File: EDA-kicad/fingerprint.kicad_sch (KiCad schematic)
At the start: 2 parts, among them J4 FINGER

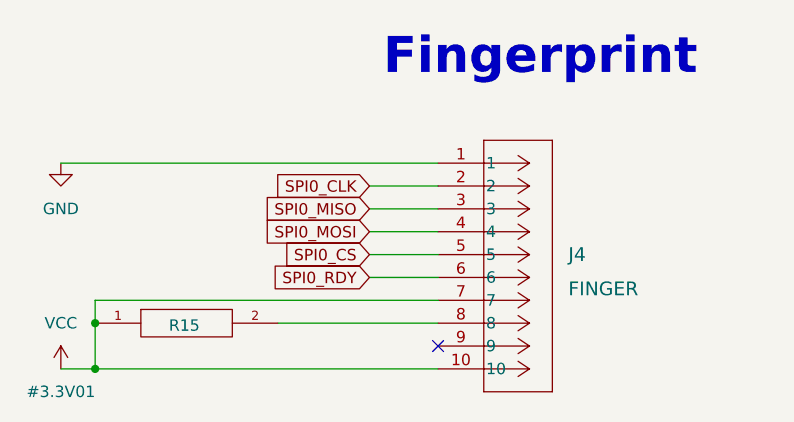
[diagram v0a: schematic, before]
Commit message: reannotate entire schematic
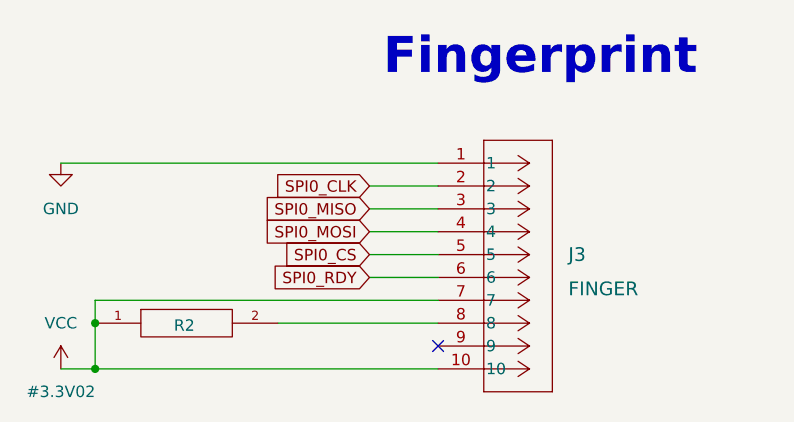
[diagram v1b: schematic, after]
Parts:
- renumbered J4 to J3, R15 to R2
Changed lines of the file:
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@@
 			"AAAAAAAAAAAAAAAAAAAAAAAAAAAAAAAAAAAAAAAAAAAAAAAAAAAAAAAAAAAAAAAAAAAAAAAAAAAA"
 			"AAAAAAAAAAAAAAAAAAAAAAAAAAAAAAAAAAAAAAAAAAAAAAAAAAAAAAAAAAAAAAAAAAAAAAAAAAAA"
-			"AAAAAAAAAAAAAAAAAAAAAAAAAAAAAAAAAAAAAAAAAAAAAAAAAAAAAA=="
+			"AAAAAAAAAAAAAAAAAAAAAAAAAAAAAAAAAAAAAAAAAAAAAAAAAAAAAAAAAFBCJC1WVQAACQAAAAAA"
+			"AAAJAAAAAAAAAEMAAABvAAAAAAAAAAAAAAAAAAAAAAAAACDDqylWVQAAFAAAAAAAAAAUAAAAAAAA"
+			"AEwAAAA3AAAAAAAAAAAAAAAAAAAAAAAAADYAAAA4AAAAkQAAAAAAAABwViQtVlUAAMAcX/oZfwAA"
+			"oFQkLVZVAACAViQtVlUAAMBJJC1WVQAACQAAAAAAAAAJAAAAAAAAAIBZa/QYfwAAAAAAAAAAAAAA"
+			"AAAAAAAAACBWJC1WVQAAAQAAAAAAAABVAAAAAAAAAEEAAABMAAAAAAAAAAAAAAAAAAAAAAAAAEAC"
+			"AAAAAAAAMAAAAAAAAAA1kEZ4U1UAAENoYXJhY3RlcgAAAGgAAABlAAAAZQAAAHQAAAAAAAAA0QcA"
+			"AAAAAABwwCMTVlUAAOCxJC1WVQAAAAAAAAAAAAAAAAAAAAAAACCf8yRWVQAABQAAAAAAAAAFAAAA"
+			"AAAAAHcAAAB3AAAAAAAAAAAAAAAAAAAAAAAAAJBTJC1WVQAADAAAAAAAAAAMAAAAAAAAAHQAAAAu"
+			"AAAAAAAAAAAAAAAAAAAAAAAAAJAAAAAAAAAAUAEAAAAAAABHAAAAcgAAAGUAAABlAAAAbgAAACAA"
+			"AABTAAAAaQAAAG4AAABnAAAAbAAAAGUAAAAtAAAAZAAAAGkAAABnAAAAaQAAAHQAAAAgAAAATgAA"
+			"AHUAAABtAAAAZQAAAHIAAABpAAAAYwAAACAAAABEAAAAaQAAAHMAAABwAAAAbAAAAGEAAAB5AAAA"
+			"IAAAAHcAAABpAAAAdAAAAGgAAAAgAAAAdwAAAGgAAABpAAAAdAAAAGUAAAAgAAAAdwAAAGgAAABp"
+			"AAAAdAAAAGUAAAAgAAAAZAAAAGkAAABmAAAAZgAAAHUAAABzAAAAZQAAAGQAAAAgAAAAbAAAAGUA"
+			"AABuAAAAcwAAACwAAAAgAAAAYwAAAG8AAABtAAAAbQAAAG8AAABuAAAAIAAAAGEAAABuAAAAbwAA"
+			"AGQAAABlAAAAAAAAAHQAAABwAAAAEQEAAAAAAACAoiQtVlUAAMCUJC1WVQAAOgAAAC8AAAAvAAAA"
+			"dwAAAHcAAAB3AAAALgAAAGsAAABpAAAAbgAAAGcAAABiAAAAcgAAAGkAAABnAAAAaAAAAHQAAAB1"
+			"AAAAcwAAAGEAAAAuAAAAYwAAAG8AAABtAAAALwAAAGkAAABtAAAAYQAAAGcAAABlAAAAcwAAAC8A"
+			"AABjAAAAYQAAAHQAAABhAAAAbAAAAG8AAABnAAAALwAAAFMAAABQAAAARQAAAEMAAAAvAAAAUwAA"
+			"AEEAAAAxAAAANQAAAC0AAAAxAAAAMQAAAEUAAABXAAAAQQAAAC4AAA=="
 		)
 	)
@@
 			"AAAAAAAAAAAAAAAAAAAAAAAAAAAAAAAAAAAAAAAAAAAAAAAAAAAAAAAAAAAAAAAAAAAAAAAAAAAA"
 			"AAAAAAAAAAAAAAAAAAAAAAAAAAAAAAAAAAAAAAAAAAAAAAAAAAAAAAAAAAAAAAAAAAAAAAAAAAAA"
+			"AAAAAAAAAAAAAAAAAAAAAAAAAAAAAAAAAAAAAAAAAAAAAAAAAAAAAAAAAAAAAAAAAAAAAAAAAAAA"
+			"AAAAAAAAAAAAAAAAAAAAAAAAAAAAAAAAAAAAAAAAAAAAAAAAAAAAAAAAAAAAAAAAAAAAAAAAAAAA"
+			"AAAAAAAAAAAAAAAAAAAAAAAAAAAAAAAAAAAAAAAAAAAAAAAAAAAAAAAAAAAAAAAAAAAAAAAAAAAA"
+			"AAAAAAAAAAAAAAAAAAAAAAAAAAAAAAAAAAAAAAAAAAAAAAAAAAAAAAAAAAAAAAAAAAAAAAAAAAAA"
+			"AAAAAAAAAAAAAAAAAAAAAAAAAAAAAAAAAAAAAAAAAAAAAAAAAAAAAAAAAAAAAAAAAAAAAAAAAAAA"
+			"AAAAAAAAAAAAAAAAAAAAAAAAAAAAAAAAAAAAAAAAAAAAAAAAAAAAAAAAAAAAAAAAAAAAAAAAAAAA"
+			"AAAAAAAAAAAAAAAAAAAAAAAAAAAAAAAAAAAAAAAAAAAAAAAAAAAAAAAAAAAAAAAAAAAAAAAAAAAA"
+			"AAAAAAAAAAAAAAAAAAAAAAAAAAAAAAAAAAAAAAAAAAAAAAAAAAAAAAAAAAAAAAAAAAAAAAAAAAAA"
+			"AAAAAAAAAAAAAAAAAAAAAAAAAAAAAAAAAAAAAAAAAAAAAAAAAAAAAAAAAAAAAAAAAAAAAAAAAAAA"
+			"AAAAAAAAAAAAAAAAAAAAAAAAAAAAAAAAAAAAAAAAAAAAAAAAAAAAAAAAAAAAAAAAAAAAAAAAAAAA"
+			"AAAAAAAAAAAAAAAAAAAAAAAAAAAAAAAAAAAAAAAAAAAAAAAAAAAAAAAAAAAAAAAAAAAAAAAAAP//"
+			"/wHh0toi4dLaIt/P3yAAAAAAAAAAAAAAAAAAAAAAAAAAAAAAAAAAAAAAAAAAAAAAAAAAAAAAAAAA"
+			"AAAAAAAAAAAAAAAAAAAAAAAAAAAAAAAAAAAAAAAAAAAAAAAAAAAAAAAAAAAAAAAAAAAAAAAAAAAA"
+			"AAAAAAAAAAAAAAAAAAAAAAAAAAAAAAAAAAAAAAAAAAAAAAAAAAAAAAAAAAAAAAAAAAAAAN7T3nre"
+			"093a3tPcqd/f3wgAAAAAAAAAAOjR6Ave093/3tPd/97T3fIAAAAAAAAAAAAAAAAAAAAAAAAAAAAA"
+			"AAAAAAAAAAAAAAAAAAAAAAAAAAAAAAAAAAAAAAAAAAAAAAAAAAAAAAAAAAAAAAAAAAAAAAAAAAAA"
+			"AAAAAAAAAAAAAAAAAAAAAAAAAAAAAAAAAAAAAAAAAAAAAAAAAAAAAAAAAAAAAAAAAAAAAAAAAAAA"
+			"AAAAAAAAAAAAAAAA////Ad7T3fje093/3tPd/+DU3EEAAAAAAAAAAOjR6Ave093/3tPd/97T3fIA"
 			"AAAAAAAAAAAAAAAAAAAAAAAAAAAAAAAAAAAAAAAAAAAAAAAAAAAAAAAAAAAAAAAAAA=="
 		)
@@
 		(dnp no)
 		(fields_autoplaced yes)
-		(property "Reference" "#PWR01"
+		(property "Reference" "#PWR065"
 			(at 87.63 100.33 0)
 			(effects
@@
 			(project "cm5-carrier"
 				(path "/28c5e4fe-1ec7-4477-97f0-d2ec1401fad5/22a7f479-b60d-43d3-acd2-a72a0c1ab82c"
-					(reference "#PWR01")
+					(reference "#PWR065")
 					(unit 1)
 				)
@@
 		(on_board yes)
 		(dnp no)
-		(property "Reference" "#3.3V01"
+		(property "Reference" "#3.3V02"
 			(at 87.63 119.38 0)
 			(effects
@@
 			(project "cm5-carrier"
 				(path "/28c5e4fe-1ec7-4477-97f0-d2ec1401fad5/22a7f479-b60d-43d3-acd2-a72a0c1ab82c"
-					(reference "#3.3V01")
+					(reference "#3.3V02")
 					(unit 1)
 				)
@@
 		(dnp no)
 		(fields_autoplaced yes)
-		(property "Reference" "J4"
+		(property "Reference" "J3"
 			(at 144.018 104.14 0)
 			(effects
@@
 			(project "cm5-carrier"
 				(path "/28c5e4fe-1ec7-4477-97f0-d2ec1401fad5/22a7f479-b60d-43d3-acd2-a72a0c1ab82c"
-					(reference "J4")
+					(reference "J3")
 					(unit 1)
 				)
@@
 		(on_board yes)
 		(dnp no)
-		(property "Reference" "R15"
+		(property "Reference" "R2"
 			(at 101.346 112.014 0)
 			(effects
@@
 			(project "cm5-carrier"
 				(path "/28c5e4fe-1ec7-4477-97f0-d2ec1401fad5/22a7f479-b60d-43d3-acd2-a72a0c1ab82c"
-					(reference "R15")
+					(reference "R2")
 					(unit 1)
 				)

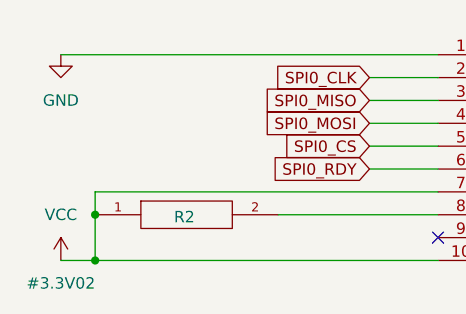
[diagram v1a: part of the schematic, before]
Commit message: add new switches and reannotate
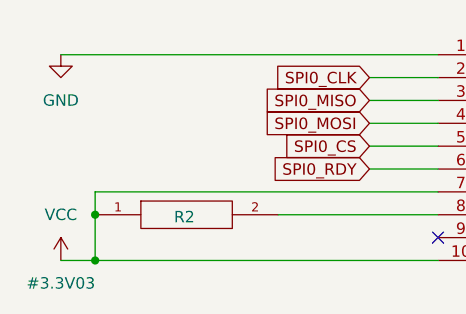
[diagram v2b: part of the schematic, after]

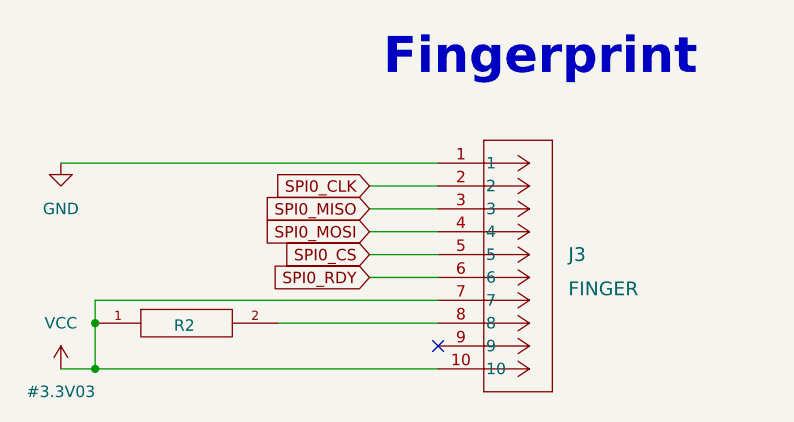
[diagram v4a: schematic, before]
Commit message: set everything except from power to DNP
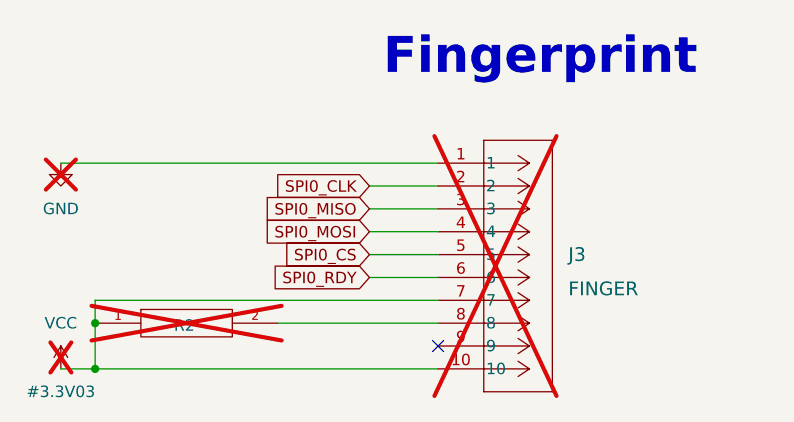
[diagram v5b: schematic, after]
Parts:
- J3, R2: now not fitted

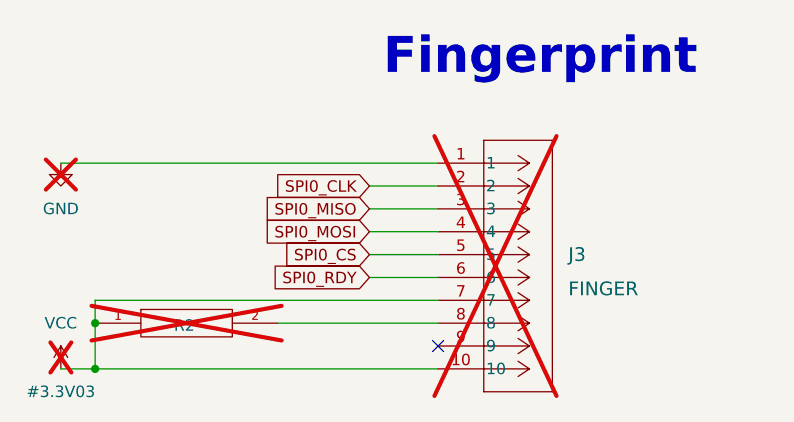
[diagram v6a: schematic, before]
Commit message: Improve KiCAD schematic design and labeling
- Replace overused global labels with hierarchical and local labels
- Add proper GND connections to components
- Fix BACKLIGHT- net issues
- Apply minor schematic fixes and cleanups
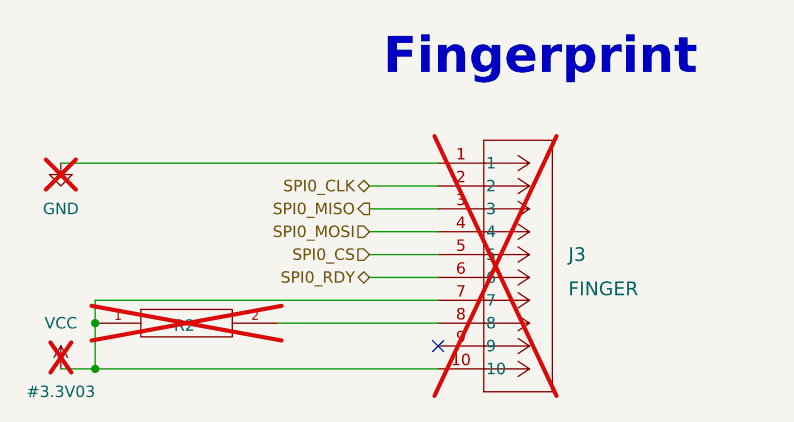
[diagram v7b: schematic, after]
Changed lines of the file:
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@@
 		)
 	)
-	(global_label "SPI0_CLK"
+	(hierarchical_label "SPI0_CS"
 		(shape input)
-		(at 121.92 96.52 180)
-		(fields_autoplaced yes)
+		(at 121.92 104.14 180)
 		(effects
 			(font
@@
 			(justify right)
 		)
-		(property "Intersheetrefs" "${INTERSHEET_REFS}"
-			(at 110.1053 96.52 0)
-			(effects
-				(font
-					(size 1.27 1.27)
-				)
-				(justify right)
-				(hide yes)
-			)
-		)
 	)
-	(global_label "SPI0_RDY"
-		(shape input)
+	(hierarchical_label "SPI0_RDY"
+		(shape bidirectional)
 		(at 121.92 106.68 180)
-		(fields_autoplaced yes)
 		(effects
 			(font
@@
 			(justify right)
 		)
-		(property "Intersheetrefs" "${INTERSHEET_REFS}"
-			(at 110.0448 106.68 0)
-			(effects
-				(font
-					(size 1.27 1.27)
-				)
-				(justify right)
-				(hide yes)
-			)
-		)
 	)
-	(global_label "SPI0_MISO"
-		(shape input)
+	(hierarchical_label "SPI0_MISO"
+		(shape output)
 		(at 121.92 99.06 180)
-		(fields_autoplaced yes)
 		(effects
 			(font
@@
 			(justify right)
 		)
-		(property "Intersheetrefs" "${INTERSHEET_REFS}"
-			(at 109.0772 99.06 0)
-			(effects
-				(font
-					(size 1.27 1.27)
-				)
-				(justify right)
-				(hide yes)
-			)
-		)
 	)
-	(global_label "SPI0_CS"
+	(hierarchical_label "SPI0_MOSI"
 		(shape input)
-		(at 121.92 104.14 180)
-		(fields_autoplaced yes)
+		(at 121.92 101.6 180)
 		(effects
 			(font
@@
 			(justify right)
 		)
-		(property "Intersheetrefs" "${INTERSHEET_REFS}"
-			(at 111.1939 104.14 0)
-			(effects
-				(font
-					(size 1.27 1.27)
-				)
-				(justify right)
-				(hide yes)
-			)
-		)
 	)
-	(global_label "SPI0_MOSI"
-		(shape input)
-		(at 121.92 101.6 180)
-		(fields_autoplaced yes)
+	(hierarchical_label "SPI0_CLK"
+		(shape bidirectional)
+		(at 121.92 96.52 180)
 		(effects
 			(font
@@
 			(justify right)
 		)
-		(property "Intersheetrefs" "${INTERSHEET_REFS}"
-			(at 109.0772 101.6 0)
-			(effects
-				(font
-					(size 1.27 1.27)
-				)
-				(justify right)
-				(hide yes)
-			)
-		)
 	)
